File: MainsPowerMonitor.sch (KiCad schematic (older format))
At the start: 25 parts, among them J401 Screw_Terminal_01x02, J402 Screw_Terminal_01x02, Q401 SSM3K329R, U401 MIC7211YM5-TR, U402 LMC7101BYM5-TR

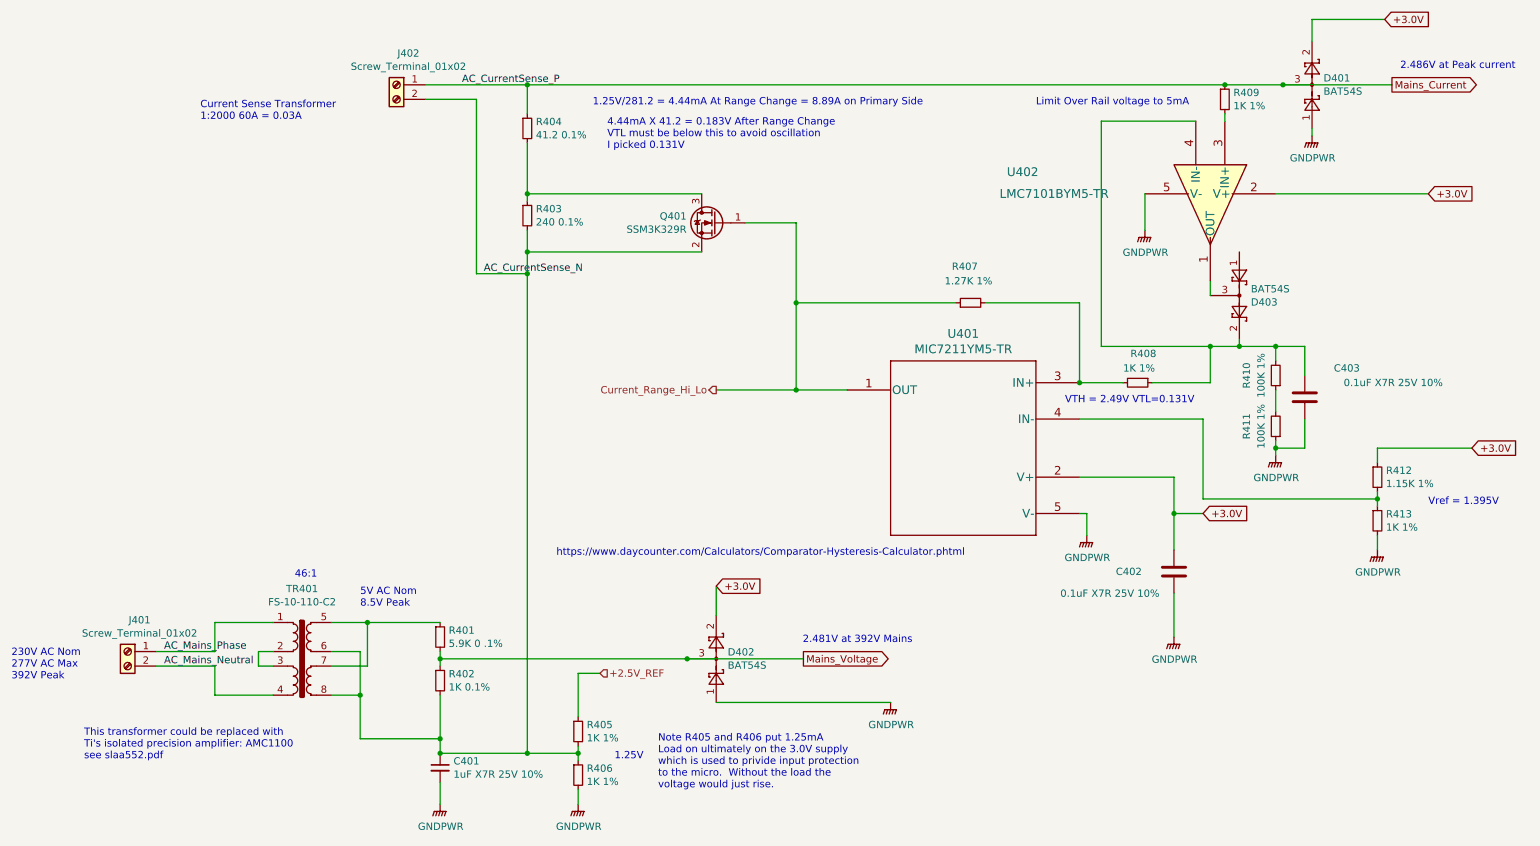
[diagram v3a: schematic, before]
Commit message: Added extra FET in Current sense Auto Ranging circuit to stop the conduction of the body diode of the single FET on the negative half of the mains cycle.  Also change the Values of all the TestPoints from TestPoint to a useful name either the voltage they should read or what they measure, also chaged there layer to front Silks so they can be used.
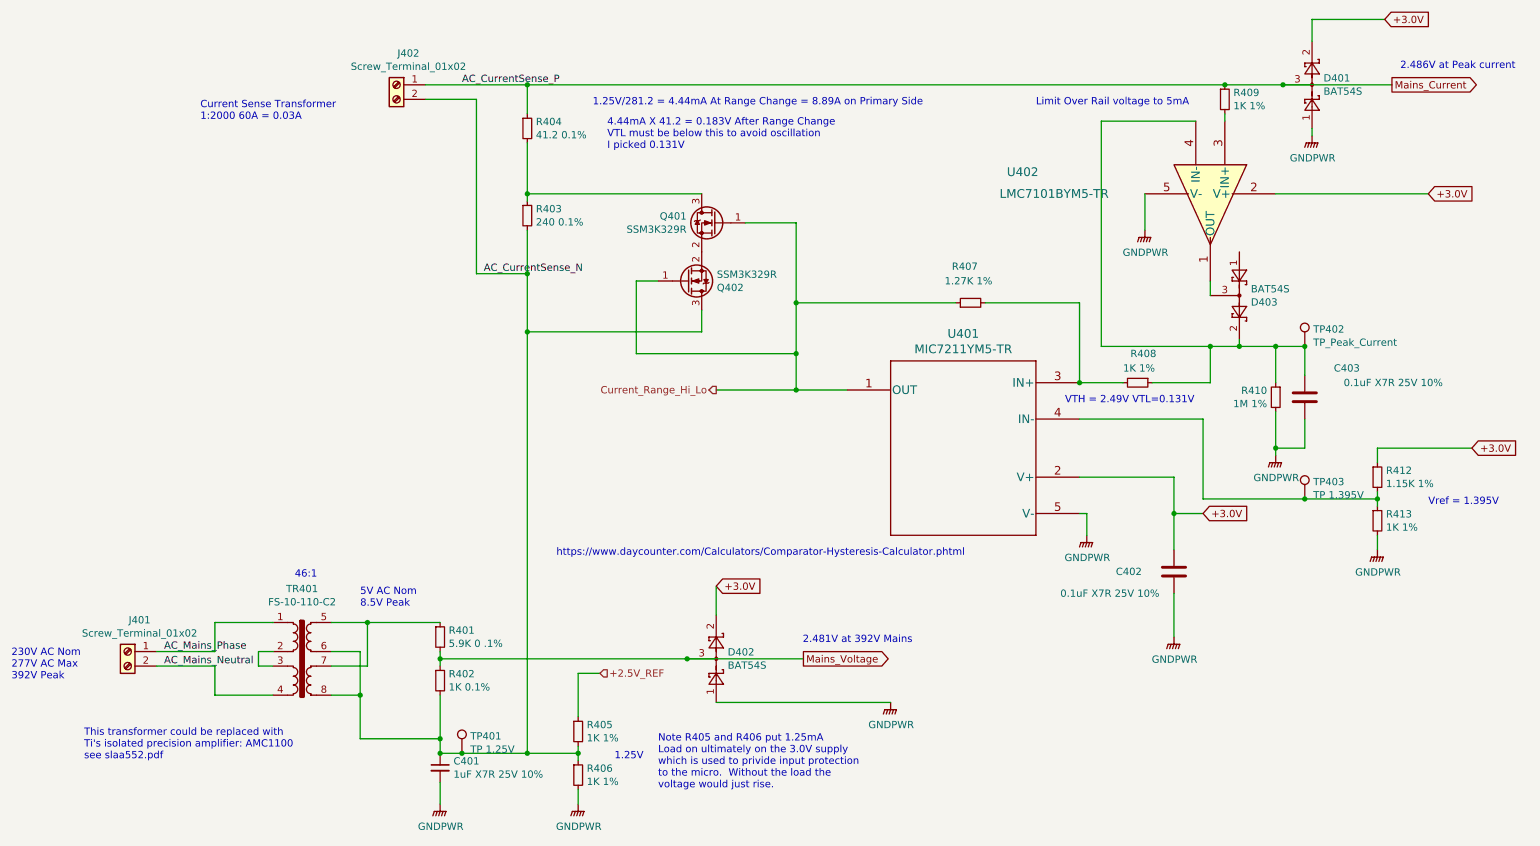
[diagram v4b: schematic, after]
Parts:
- removed R411: 100K 1%, Resistor_SMD:R_0805_2012Metric_Pad1.15x1.40mm_HandSolder, symbol Device:R_Small
- added Q402: SSM3K329R, Package_TO_SOT_SMD:SOT-23_Handsoldering, symbol Device:Q_NMOS_GSD
- added TP401: TP 1.25V, TestPoint:TestPoint_Pad_3.0x3.0mm, symbol Connector:TestPoint
- added TP402: TP_Peak_Current, TestPoint:TestPoint_Pad_3.0x3.0mm, symbol Connector:TestPoint
- added TP403: TP 1.395V, TestPoint:TestPoint_Pad_3.0x3.0mm, symbol Connector:TestPoint
- R410: value 100K 1% -> 1M 1%; MPN RC0805FR-07100KL -> RC0805FR-071ML; SPN 311-100KCRCT-ND -> 311-1.00MCRCT-ND
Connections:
- net AC_CurrentSense_N: now also Q402.3 (D), TP401.1; no longer Q401.2 (S)
- net Current_Range_Hi_Lo: now also Q402.1 (G)
- net GNDPWR: now also R410.2
- net at R412.2, R413.1, U401.4 (IN-): now also TP403.1
- net at C403.1, D403.2, R408.1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: now also R410.1, TP402.1; no longer R410.2
- new net: Q401.2 (S), Q402.2 (S)
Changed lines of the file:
@@
-$EndComp
-$Comp
-L Device:R_Small R?
-U 1 1 5F65A3B7
-P 9400 3700
-AR Path="/5EF73D52/5F65A3B7" Ref="R?"  Part="1"
-AR Path="/5F15BF3C/5F65A3B7" Ref="R410"  Part="1"
-F 0 "R410" V 9600 3700 50  0000 C CNN
-F 1 "100K 1%" V 9500 3700 50  0000 C CNN
-F 2 "Resistor_SMD:R_0805_2012Metric_Pad1.15x1.40mm_HandSolder" H 9400 3700 50  0001 C CNN
-F 3 "https://www.yageo.com/upload/media/product/productsearch/datasheet/rchip/PYu-RC_Group_51_RoHS_L_11.pdf" H 9400 3700 50  0001 C CNN
-F 4 "Yageo" H 7750 1100 50  0001 C CNN "MFR"
-F 5 "RC0805FR-07100KL" H 7750 1100 50  0001 C CNN "MPN"
-F 6 "digikey" H 7750 1100 50  0001 C CNN "SPR"
-F 7 "311-100KCRCT-ND" H 7750 1100 50  0001 C CNN "SPN"
-F 8 "-" H 7750 1100 50  0001 C CNN "SPURL"
-	1    9400 3700
-	-1   0    0    1
 $EndComp
 $Comp
@@
 	1    10100 4900
 	1    0    0    -1
-$EndComp
-$Comp
-L Device:R_Small R?
-U 1 1 5F8DBFA7
-P 9400 4050
-AR Path="/5EF73D52/5F8DBFA7" Ref="R?"  Part="1"
-AR Path="/5F15BF3C/5F8DBFA7" Ref="R411"  Part="1"
-F 0 "R411" V 9600 4050 50  0000 C CNN
-F 1 "100K 1%" V 9500 4050 50  0000 C CNN
-F 2 "Resistor_SMD:R_0805_2012Metric_Pad1.15x1.40mm_HandSolder" H 9400 4050 50  0001 C CNN
-F 3 "https://www.yageo.com/upload/media/product/productsearch/datasheet/rchip/PYu-RC_Group_51_RoHS_L_11.pdf" H 9400 4050 50  0001 C CNN
-F 4 "Yageo" H 7750 1450 50  0001 C CNN "MFR"
-F 5 "RC0805FR-07100KL" H 7750 1450 50  0001 C CNN "MPN"
-F 6 "digikey" H 7750 1450 50  0001 C CNN "SPR"
-F 7 "311-100KCRCT-ND" H 7750 1450 50  0001 C CNN "SPN"
-F 8 "-" H 7750 1450 50  0001 C CNN "SPURL"
-	1    9400 4050
-	-1   0    0    1
 $EndComp
 Text Notes 700  5800 0    50   ~ 0
@@
 	3900 3000 4250 3000
 Wire Wire Line
-	4250 3000 4250 6300
+	4250 3000 4250 3400
 Wire Wire Line
 	3550 1700 4250 1700
 Wire Wire Line
-	3650 6300 4250 6300
+	3650 6300 3800 6300
 Wire Wire Line
 	4250 6300 4600 6300
 Wire Wire Line
-	4250 3000 4250 2850
-Wire Wire Line
 	4250 2100 4250 2450
 Wire Wire Line
@@
 	4250 2450 4250 2500
 Wire Wire Line
-	5450 2850 4250 2850
-Wire Wire Line
-	4250 2850 4250 2700
-Wire Wire Line
 	8700 4900 8700 4650
 Wire Wire Line
@@
 	6450 3800 6100 3800
 Wire Wire Line
-	6100 3800 6100 3200
+	6100 3800 6100 3550
 Wire Wire Line
 	6100 2650 5750 2650
@@
 	9150 3500 9400 3500
 Wire Wire Line
-	9400 3500 9400 3600
-Wire Wire Line
 	9400 3500 9600 3500
 Wire Wire Line
@@
 	8950 3500 8200 3500
 Wire Wire Line
-	9400 3800 9400 3950
-Wire Wire Line
-	9400 4150 9400 4200
-Wire Wire Line
 	9600 3500 9600 3700
 Wire Wire Line
@@
 	8900 4000 8050 4000
 Wire Wire Line
-	8900 4550 10100 4550
+	8900 4550 9600 4550
 Connection ~ 3150 5400
 Connection ~ 3100 5900
@@
 Connection ~ 4250 6300
 Connection ~ 4250 2450
-Connection ~ 4250 2850
 Connection ~ 8700 4650
 Connection ~ 4250 1700
@@
 	6100 3800 5550 3800
 Connection ~ 6100 3800
+$Comp
+L Device:R_Small R?
+U 1 1 5F9F2143
+P 9400 3850
+AR Path="/5F9F2143" Ref="R?"  Part="1"
+AR Path="/5F15BF3C/5F9F2143" Ref="R410"  Part="1"
+F 0 "R410" H 9459 3896 50  0000 L CNN
+F 1 "1M 1%" H 9459 3805 50  0000 L CNN
+F 2 "Resistor_SMD:R_0805_2012Metric_Pad1.15x1.40mm_HandSolder" H 9400 3850 50  0001 C CNN
+F 3 "https://www.yageo.com/upload/media/product/productsearch/datasheet/rchip/PYu-RC_Group_51_RoHS_L_11.pdf" H 9400 3850 50  0001 C CNN
+F 4 "Yageo" H 2650 -2050 50  0001 C CNN "MFR"
+F 5 "RC0805FR-071ML" H 2650 -2050 50  0001 C CNN "MPN"
+F 6 "digikey" H 2650 -2050 50  0001 C CNN "SPR"
+F 7 "311-1.00MCRCT-ND" H 2650 -2050 50  0001 C CNN "SPN"
+F 8 "-" H 2650 -2050 50  0001 C CNN "SPURL"
+	1    9400 3850
+	-1   0    0    -1
+$EndComp
+Wire Wire Line
+	9400 3500 9400 3750
+Wire Wire Line
+	9400 3950 9400 4200
+$Comp
+L Device:Q_NMOS_GSD Q?
+U 1 1 5F9FF42A
+P 5350 3050
+AR Path="/5F9FF42A" Ref="Q?"  Part="1"
+AR Path="/5F15BF3C/5F9FF42A" Ref="Q402"  Part="1"
+F 0 "Q402" H 5554 3096 50  0000 L CNN
+F 1 "SSM3K329R" H 5554 3005 50  0000 L CNN
+F 2 "Package_TO_SOT_SMD:SOT-23_Handsoldering" H 5550 3150 50  0001 C CNN
+F 3 "https://toshiba.semicon-storage.com/info/docget.jsp?did=2157&prodName=SSM3K329R" H 5350 3050 50  0001 C CNN
+F 4 "Toshiba Semiconductor and Storage" H -1150 -3600 50  0001 C CNN "MFR"
+F 5 "SSM3K329R,LF" H -1150 -3600 50  0001 C CNN "MPN"
+F 6 "digikey" H -1150 -3600 50  0001 C CNN "SPR"
+F 7 "SSM3K329RLFCT-ND" H -1150 -3600 50  0001 C CNN "SPN"
+F 8 "-" H -1150 -3600 50  0001 C CNN "SPURL"
+	1    5350 3050
+	1    0    0    1
+$EndComp
+Wire Wire Line
+	4250 2700 4250 3000
+Wire Wire Line
+	5450 3250 5450 3400
+Wire Wire Line
+	5450 3400 4250 3400
+Connection ~ 4250 3400
+Wire Wire Line
+	4250 3400 4250 6300
+Wire Wire Line
+	5150 3050 5000 3050
+Wire Wire Line
+	5000 3050 5000 3550
+Wire Wire Line
+	5000 3550 6100 3550
+Connection ~ 6100 3550
+Wire Wire Line
+	6100 3550 6100 3200
+$Comp
+L Connector:TestPoint TP?
+U 1 1 5FA2A174
+P 9600 4550
+AR Path="/5EBD6442/5FA2A174" Ref="TP?"  Part="1"
+AR Path="/5EF73D52/5FA2A174" Ref="TP?"  Part="1"
+AR Path="/5FA2A174" Ref="TP?"  Part="1"
+AR Path="/5F15BF3C/5FA2A174" Ref="TP403"  Part="1"
+F 0 "TP403" H 9658 4668 50  0000 L CNN
+F 1 "TP 1.395V" H 9658 4577 50  0000 L CNN
+F 2 "TestPoint:TestPoint_Pad_3.0x3.0mm" H 9800 4550 50  0001 C CNN
+F 3 "~" H 9800 4550 50  0001 C CNN
+F 4 "-" H 8150 -1750 50  0001 C CNN "MFR"
+F 5 "-" H 8150 -1750 50  0001 C CNN "MPN"
+F 6 "-" H 8150 -1750 50  0001 C CNN "SPR"
+F 7 "-" H 8150 -1750 50  0001 C CNN "SPN"
+F 8 "-" H 8150 -1750 50  0001 C CNN "SPURL"
+	1    9600 4550
+	1    0    0    -1
+$EndComp
+Connection ~ 9600 4550
+Wire Wire Line
+	9600 4550 10100 4550
+$Comp
+L Connector:TestPoint TP?
+U 1 1 5FA32312
+P 3800 6300
+AR Path="/5EBD6442/5FA32312" Ref="TP?"  Part="1"
+AR Path="/5EF73D52/5FA32312" Ref="TP?"  Part="1"
+AR Path="/5FA32312" Ref="TP?"  Part="1"
+AR Path="/5F15BF3C/5FA32312" Ref="TP401"  Part="1"
+F 0 "TP401" H 3858 6418 50  0000 L CNN
+F 1 "TP 1.25V" H 3858 6327 50  0000 L CNN
+F 2 "TestPoint:TestPoint_Pad_3.0x3.0mm" H 4000 6300 50  0001 C CNN
+F 3 "~" H 4000 6300 50  0001 C CNN
+F 4 "-" H 2350 0   50  0001 C CNN "MFR"
+F 5 "-" H 2350 0   50  0001 C CNN "MPN"
+F 6 "-" H 2350 0   50  0001 C CNN "SPR"
+F 7 "-" H 2350 0   50  0001 C CNN "SPN"
+F 8 "-" H 2350 0   50  0001 C CNN "SPURL"
+	1    3800 6300
+	1    0    0    -1
+$EndComp
+Connection ~ 3800 6300
+Wire Wire Line
+	3800 6300 4250 6300
+$Comp
+L Connector:TestPoint TP?
+U 1 1 5FA3BECA
+P 9600 3500
+AR Path="/5EBD6442/5FA3BECA" Ref="TP?"  Part="1"
+AR Path="/5EF73D52/5FA3BECA" Ref="TP?"  Part="1"
+AR Path="/5FA3BECA" Ref="TP?"  Part="1"
+AR Path="/5F15BF3C/5FA3BECA" Ref="TP402"  Part="1"
+F 0 "TP402" H 9658 3618 50  0000 L CNN
+F 1 "TP_Peak_Current" H 9658 3527 50  0000 L CNN
+F 2 "TestPoint:TestPoint_Pad_3.0x3.0mm" H 9800 3500 50  0001 C CNN
+F 3 "~" H 9800 3500 50  0001 C CNN
+F 4 "-" H 8150 -2800 50  0001 C CNN "MFR"
+F 5 "-" H 8150 -2800 50  0001 C CNN "MPN"
+F 6 "-" H 8150 -2800 50  0001 C CNN "SPR"
+F 7 "-" H 8150 -2800 50  0001 C CNN "SPN"
+F 8 "-" H 8150 -2800 50  0001 C CNN "SPURL"
+	1    9600 3500
+	1    0    0    -1
+$EndComp
+Connection ~ 9600 3500
 $EndSCHEMATC

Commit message: increased some trace sizes, moved some Front mask items, and generated the Gerber files, and submited order to jlcpcb, only order 1 oz copper but should be 2 oz due the the 20A charging part of the circuit, but i'll just solder some exta wire under those tracks during testing. Needs to be 9.85mm for 30deg C rise over ambient.
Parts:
- R412: SPN 311-1.00KCRCT-ND -> 311-1.15KCRCT-ND
